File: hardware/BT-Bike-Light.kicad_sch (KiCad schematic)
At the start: 25 parts, among them J1 Conn_ARM_JTAG_SWD_10, J2 USB_C_Receptacle_USB2.0_16P, Q1 Q_NMOS_GDS, SW1 SW_Push, U1 BC805M, U2 LIS2DTW12, U3 PAM2808

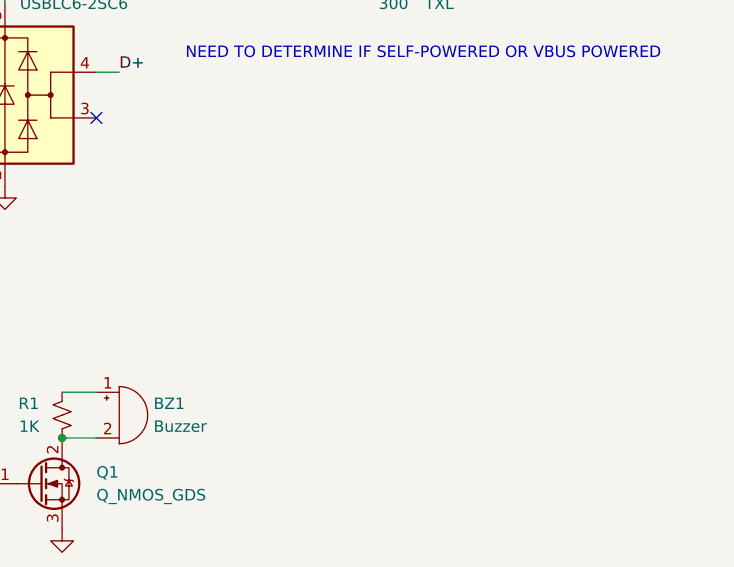
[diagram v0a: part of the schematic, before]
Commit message: Add battery protection IC
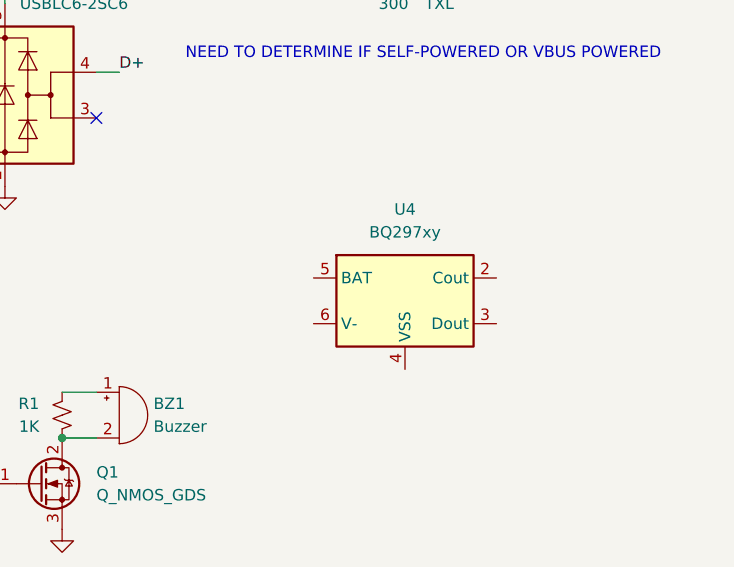
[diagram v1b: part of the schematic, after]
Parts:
- added U4: BQ297xy, Package_SON:WSON-6_1.5x1.5mm_P0.5mm, symbol Battery_Management:BQ297xy
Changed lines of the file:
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@@
+	)
+	(symbol
+		(lib_id "Battery_Management:BQ297xy")
+		(at 237.49 119.38 0)
+		(unit 1)
+		(exclude_from_sim no)
+		(in_bom yes)
+		(on_board yes)
+		(dnp no)
+		(fields_autoplaced yes)
+		(property "Reference" "U4"
+			(at 237.49 109.22 0)
+			(effects
+				(font
+					(size 1.27 1.27)
+				)
+			)
+		)
+		(property "Value" "BQ297xy"
+			(at 237.49 111.76 0)
+			(effects
+				(font
+					(size 1.27 1.27)
+				)
+			)
+		)
+		(property "Footprint" "Package_SON:WSON-6_1.5x1.5mm_P0.5mm"
+			(at 237.49 110.49 0)
+			(effects
+				(font
+					(size 1.27 1.27)
+				)
+				(hide yes)
+			)
+		)
+		(property "Datasheet" "http://www.ti.com/lit/ds/symlink/bq2970.pdf"
+			(at 231.14 114.3 0)
+			(effects
+				(font
+					(size 1.27 1.27)
+				)
+				(hide yes)
+			)
+		)
+		(property "Description" "Voltage and Current Protection for Single-Cell Li-Ion and Li-Polymer Batteries"
+			(at 237.49 119.38 0)
+			(effects
+				(font
+					(size 1.27 1.27)
+				)
+				(hide yes)
+			)
+		)
+		(pin "5"
+		)
+		(pin "1"
+		)
+		(pin "2"
+		)
+		(pin "4"
+		)
+		(pin "3"
+		)
+		(pin "6"
+		)
+		(instances
+			(project ""
+				(path "/3263b444-391f-435a-aeab-6f7fca8830e2"
+					(reference "U4")
+					(unit 1)
+				)
+			)
+		)
 	)
 	(symbol

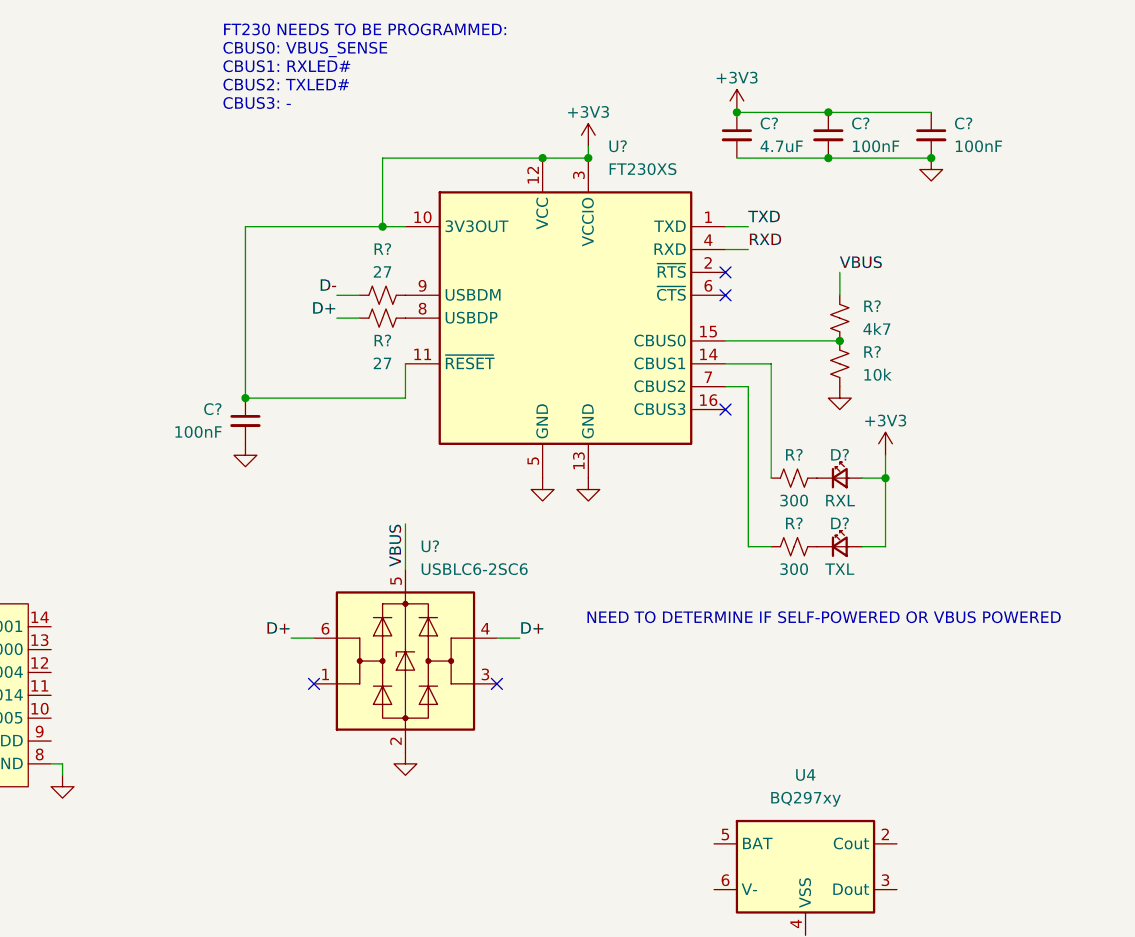
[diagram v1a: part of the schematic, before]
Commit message: Remove USB/UART bridge
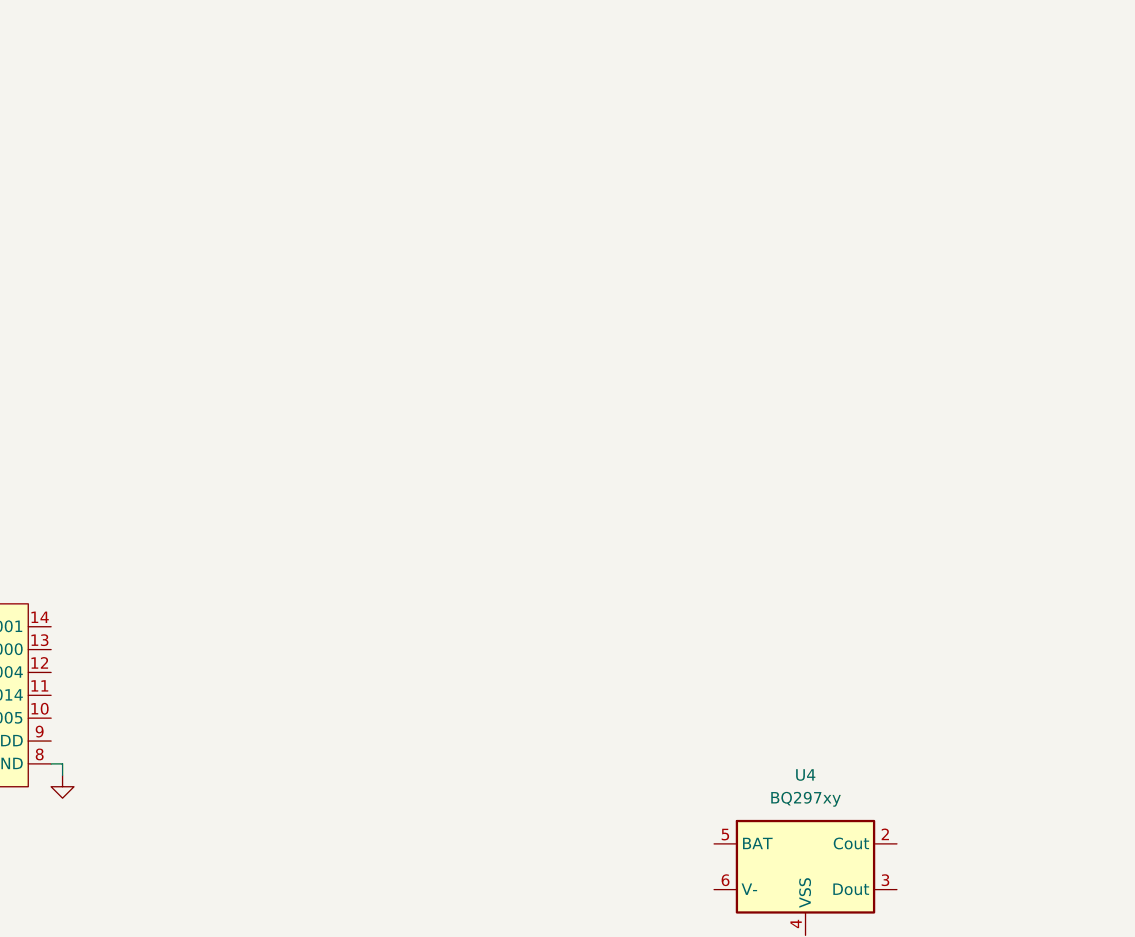
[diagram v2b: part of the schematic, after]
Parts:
- removed C?: 4.7uF, Capacitor_SMD:C_0805_2012Metric_Pad1.18x1.45mm_HandSolder, symbol Device:C_Small
- removed C? (x3): 100nF, Capacitor_SMD:C_0805_2012Metric_Pad1.18x1.45mm_HandSolder, symbol Device:C_Small
- removed D?: RXL, LED_SMD:LED_0805_2012Metric_Pad1.15x1.40mm_HandSolder, symbol Device:LED_Small
- removed D?: TXL, LED_SMD:LED_0805_2012Metric_Pad1.15x1.40mm_HandSolder, symbol Device:LED_Small
- removed R? (x2): 27, Resistor_SMD:R_0805_2012Metric_Pad1.20x1.40mm_HandSolder, symbol Device:R_Small_US
- removed R?: 4k7, Resistor_SMD:R_0805_2012Metric_Pad1.20x1.40mm_HandSolder, symbol Device:R_Small_US
- removed R? (x2): 300, Resistor_SMD:R_0805_2012Metric_Pad1.20x1.40mm_HandSolder, symbol Device:R_Small_US
- removed R?: 10k, Resistor_SMD:R_0805_2012Metric_Pad1.20x1.40mm_HandSolder, symbol Device:R_Small_US
- removed U?: FT230XS, Package_SO:SSOP-16_3.9x4.9mm_P0.635mm, symbol Interface_USB:FT230XS
- removed U?: USBLC6-2SC6, Package_TO_SOT_SMD:SOT-23-6, symbol Power_Protection:USBLC6-2SC6
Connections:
- no-connect marks 8 -> 3
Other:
- note removed: "FT230 NEEDS TO BE PROGRAMMED: CBUS0: VBUS_SENSE CBUS1: RXLED# CBUS2: TXLED# CBUS3: -"
- note removed: "NEED TO DETERMINE IF SELF-POWERED OR VBUS POWERED"

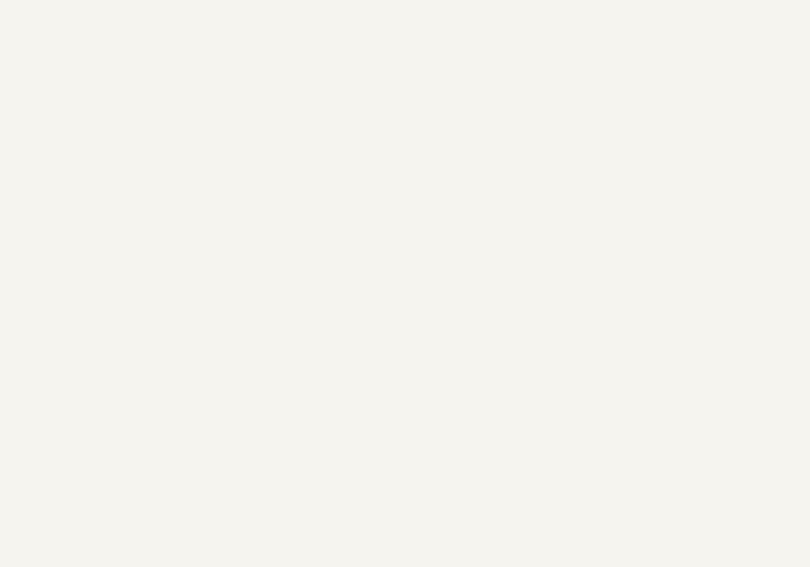
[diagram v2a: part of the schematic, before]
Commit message: Add battery charger
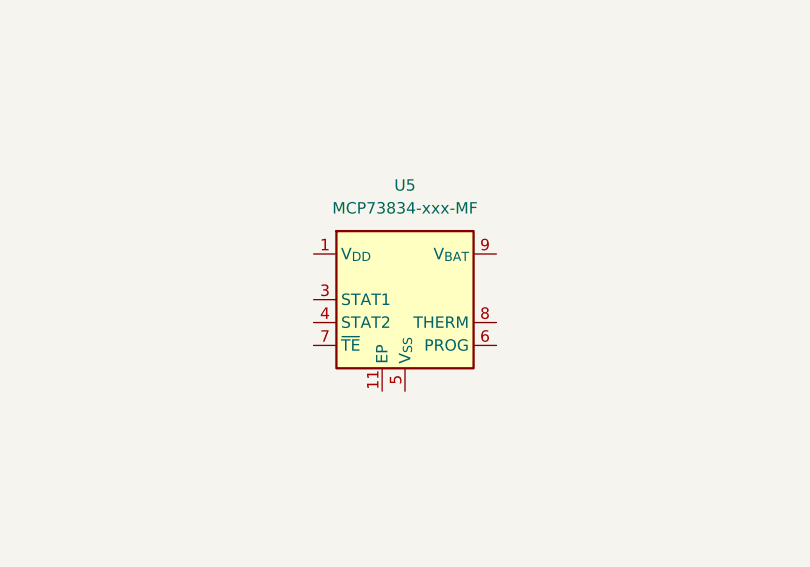
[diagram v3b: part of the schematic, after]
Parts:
- added U5: MCP73834-xxx-MF, Package_DFN_QFN:DFN-10-1EP_3x3mm_P0.5mm_EP1.58x2.35mm, symbol Microchip:MCP73834-xxx-MF
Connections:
- new net: U5.1 (V_{DD}), U5.2 (V_{DD})
- new net: U5.10 (V_{BAT}), U5.9 (V_{BAT})
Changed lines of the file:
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@@
+	)
+	(symbol
+		(lib_id "Microchip:MCP73834-xxx-MF")
+		(at 201.93 74.93 0)
+		(unit 1)
+		(exclude_from_sim no)
+		(in_bom yes)
+		(on_board yes)
+		(dnp no)
+		(fields_autoplaced yes)
+		(property "Reference" "U5"
+			(at 201.93 62.23 0)
+			(effects
+				(font
+					(size 1.27 1.27)
+				)
+			)
+		)
+		(property "Value" "MCP73834-xxx-MF"
+			(at 201.93 64.77 0)
+			(effects
+				(font
+					(size 1.27 1.27)
+				)
+			)
+		)
+		(property "Footprint" "Package_DFN_QFN:DFN-10-1EP_3x3mm_P0.5mm_EP1.58x2.35mm"
+			(at 234.95 83.82 0)
+			(effects
+				(font
+					(size 1.27 1.27)
+				)
+				(hide yes)
+			)
+		)
+		(property "Datasheet" "https://ww1.microchip.com/downloads/en/DeviceDoc/22005b.pdf"
+			(at 201.93 74.93 0)
+			(effects
+				(font
+					(size 1.27 1.27)
+				)
+				(hide yes)
+			)
+		)
+		(property "Description" "Stand-Alone Linear Li-Ion / Li-Polymer Charge Management Controller, DFN-10"
+			(at 201.93 74.93 0)
+			(effects
+				(font
+					(size 1.27 1.27)
+				)
+				(hide yes)
+			)
+		)
+		(pin "7"
+		)
+		(pin "9"
+		)
+		(pin "6"
+		)
+		(pin "5"
+		)
+		(pin "11"
+		)
+		(pin "10"
+		)
+		(pin "1"
+		)
+		(pin "8"
+		)
+		(pin "2"
+		)
+		(pin "4"
+		)
+		(pin "3"
+		)
+		(instances
+			(project ""
+				(path "/3263b444-391f-435a-aeab-6f7fca8830e2"
+					(reference "U5")
+					(unit 1)
+				)
+			)
+		)
 	)
 	(symbol

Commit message: Add LDO
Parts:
- added U6: TPS7A02, Package_TO_SOT_SMD:SOT-23-5, symbol Texas-Instruments:TPS7A02
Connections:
- net GND: now also U6.2 (GND)
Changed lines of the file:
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@@
+	)
+	(symbol
+		(lib_id "Texas-Instruments:TPS7A02")
+		(at 184.15 40.64 0)
+		(unit 1)
+		(exclude_from_sim no)
+		(in_bom yes)
+		(on_board yes)
+		(dnp no)
+		(fields_autoplaced yes)
+		(property "Reference" "U6"
+			(at 184.15 31.75 0)
+			(effects
+				(font
+					(size 1.27 1.27)
+				)
+			)
+		)
+		(property "Value" "TPS7A02"
+			(at 184.15 34.29 0)
+			(effects
+				(font
+					(size 1.27 1.27)
+				)
+			)
+		)
+		(property "Footprint" "Package_TO_SOT_SMD:SOT-23-5"
+			(at 184.15 32.385 0)
+			(effects
+				(font
+					(size 1.27 1.27)
+				)
+				(hide yes)
+			)
+		)
+		(property "Datasheet" "https://www.ti.com/lit/ds/symlink/tps7a02.pdf"
+			(at 184.15 40.64 0)
+			(effects
+				(font
+					(size 1.27 1.27)
+				)
+				(hide yes)
+			)
+		)
+		(property "Description" "TPS7A02 Nanopower IQ, 25-nA, 200-mA, Low-Dropout Voltage Regulator With Fast Transient Response"
+			(at 184.15 40.64 0)
+			(effects
+				(font
+					(size 1.27 1.27)
+				)
+				(hide yes)
+			)
+		)
+		(pin "2"
+		)
+		(pin "3"
+		)
+		(pin "4"
+		)
+		(pin "5"
+		)
+		(pin "1"
+		)
+		(instances
+			(project ""
+				(path "/3263b444-391f-435a-aeab-6f7fca8830e2"
+					(reference "U6")
+					(unit 1)
+				)
+			)
+		)
 	)
 	(symbol
@@
 					(unit 1)
 				)
+			)
+		)
+	)
+	(symbol
+		(lib_id "power:GND")
+		(at 184.15 48.26 0)
+		(unit 1)
+		(exclude_from_sim no)
+		(in_bom yes)
+		(on_board yes)
+		(dnp no)
+		(fields_autoplaced yes)
+		(property "Reference" "#PWR05"
+			(at 184.15 54.61 0)
+			(effects
+				(font
+					(size 1.27 1.27)
+				)
+				(hide yes)
+			)
+		)
+		(property "Value" "GND"
+			(at 184.15 53.34 0)
+			(effects
+				(font
+					(size 1.27 1.27)
+				)
+				(hide yes)
+			)
+		)
+		(property "Footprint" ""
+			(at 184.15 48.26 0)
+			(effects
+				(font
+					(size 1.27 1.27)
+				)
+				(hide yes)
+			)
+		)
+		(property "Datasheet" ""
+			(at 184.15 48.26 0)
+			(effects
+				(font
+					(size 1.27 1.27)
+				)
+				(hide yes)
+			)
+		)
+		(property "Description" "Power symbol creates a global label with name \"GND\" , ground"
+			(at 184.15 48.26 0)
+			(effects
+				(font
+					(size 1.27 1.27)
+				)
+				(hide yes)
+			)
+		)
+		(pin "1"
+		)
+		(instances
+			(project "BT-Bike-Light"
+				(path "/3263b444-391f-435a-aeab-6f7fca8830e2"
+					(reference "#PWR05")
+					(unit 1)
+				)

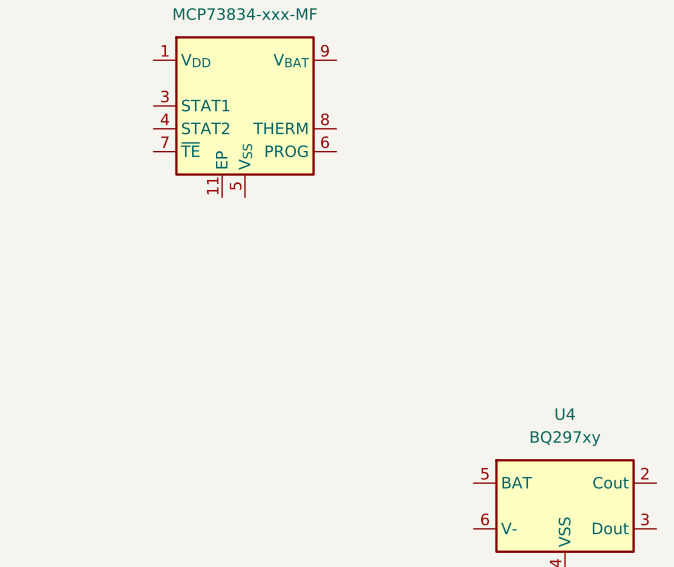
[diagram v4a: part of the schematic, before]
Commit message: Add battery connector
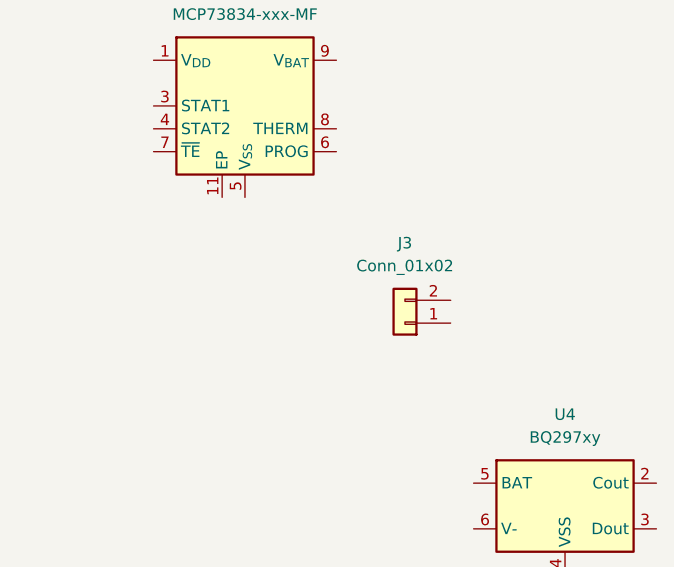
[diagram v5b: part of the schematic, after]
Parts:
- added J3: Conn_01x02, symbol Connector_Generic:Conn_01x02
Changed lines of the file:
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@@
+	)
+	(symbol
+		(lib_id "Connector_Generic:Conn_01x02")
+		(at 219.71 99.06 180)
+		(unit 1)
+		(exclude_from_sim no)
+		(in_bom yes)
+		(on_board yes)
+		(dnp no)
+		(fields_autoplaced yes)
+		(property "Reference" "J3"
+			(at 219.71 90.17 0)
+			(effects
+				(font
+					(size 1.27 1.27)
+				)
+			)
+		)
+		(property "Value" "Conn_01x02"
+			(at 219.71 92.71 0)
+			(effects
+				(font
+					(size 1.27 1.27)
+				)
+			)
+		)
+		(property "Footprint" ""
+			(at 219.71 99.06 0)
+			(effects
+				(font
+					(size 1.27 1.27)
+				)
+				(hide yes)
+			)
+		)
+		(property "Datasheet" "~"
+			(at 219.71 99.06 0)
+			(effects
+				(font
+					(size 1.27 1.27)
+				)
+				(hide yes)
+			)
+		)
+		(property "Description" "Generic connector, single row, 01x02, script generated (kicad-library-utils/schlib/autogen/connector/)"
+			(at 219.71 99.06 0)
+			(effects
+				(font
+					(size 1.27 1.27)
+				)
+				(hide yes)
+			)
+		)
+		(pin "2"
+		)
+		(pin "1"
+		)
+		(instances
+			(project ""
+				(path "/3263b444-391f-435a-aeab-6f7fca8830e2"
+					(reference "J3")
+					(unit 1)
+				)
+			)
+		)
 	)
 	(symbol
